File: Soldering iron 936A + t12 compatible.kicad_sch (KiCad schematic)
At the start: 120 parts, among them J1 DC INPUT, J10 Conn_01x01_Socket, J11 Conn_01x01_Socket, J2 USB TO SERIAL, J3 AC input, J4 output_connector, J5 mosfet_driver_future_backup, J6 OLED, J7 USB C BREAKOUT BOARD, J8 Conn_01x01_Socket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

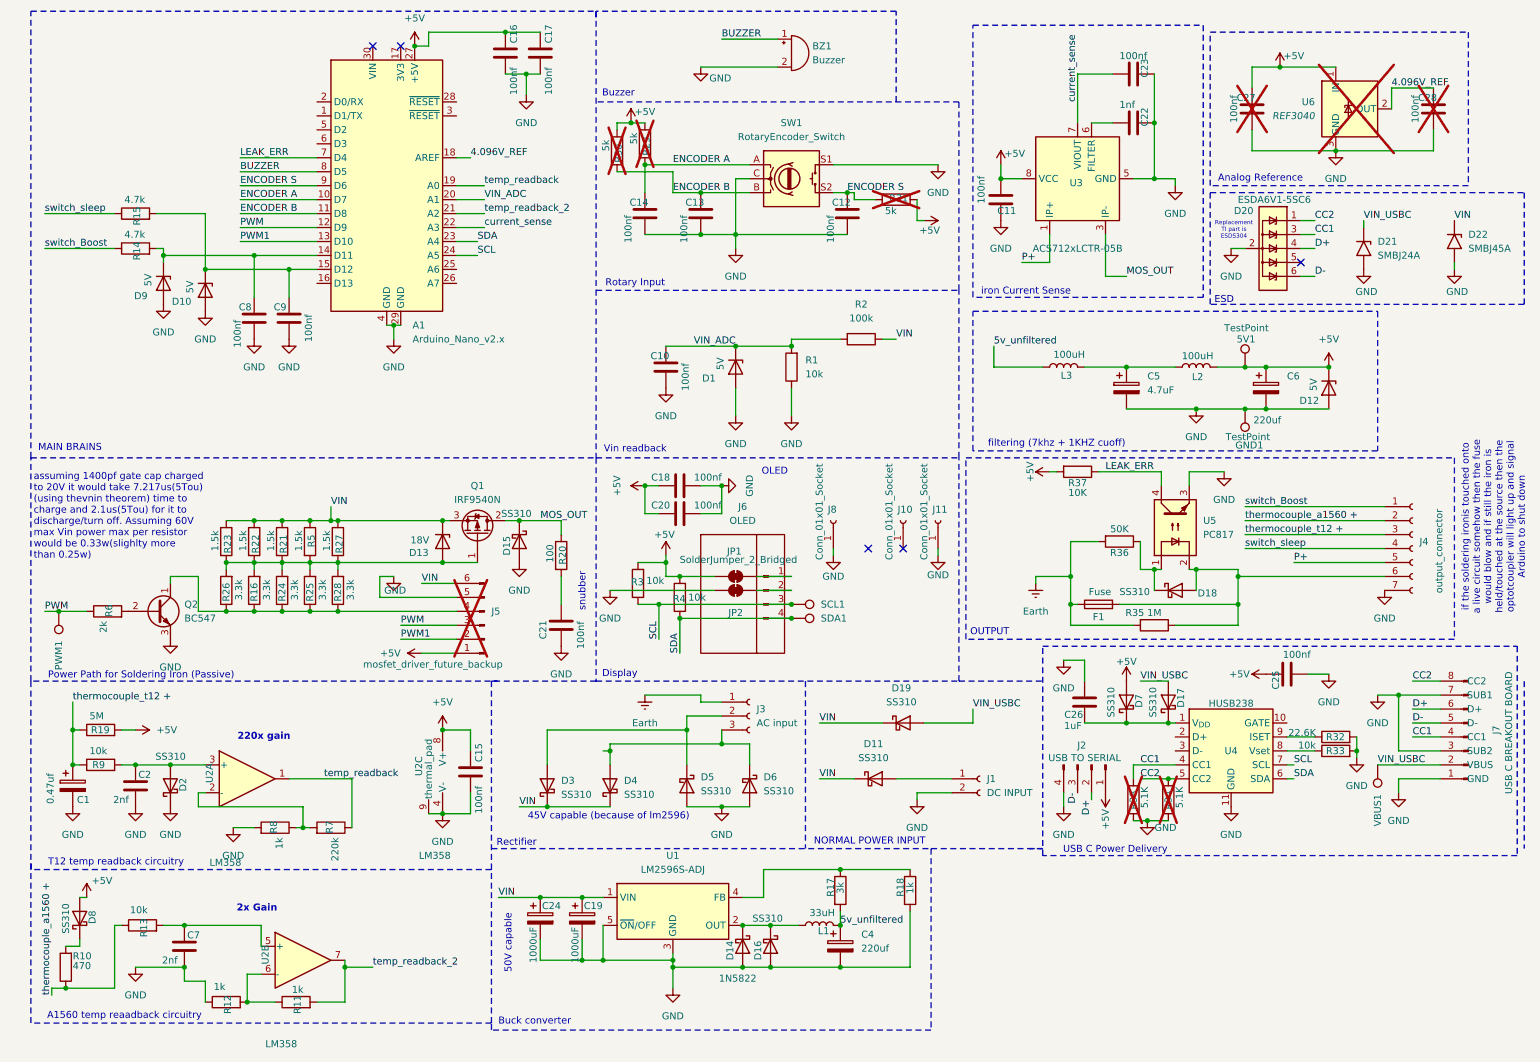
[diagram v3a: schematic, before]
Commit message: Added castellated edges
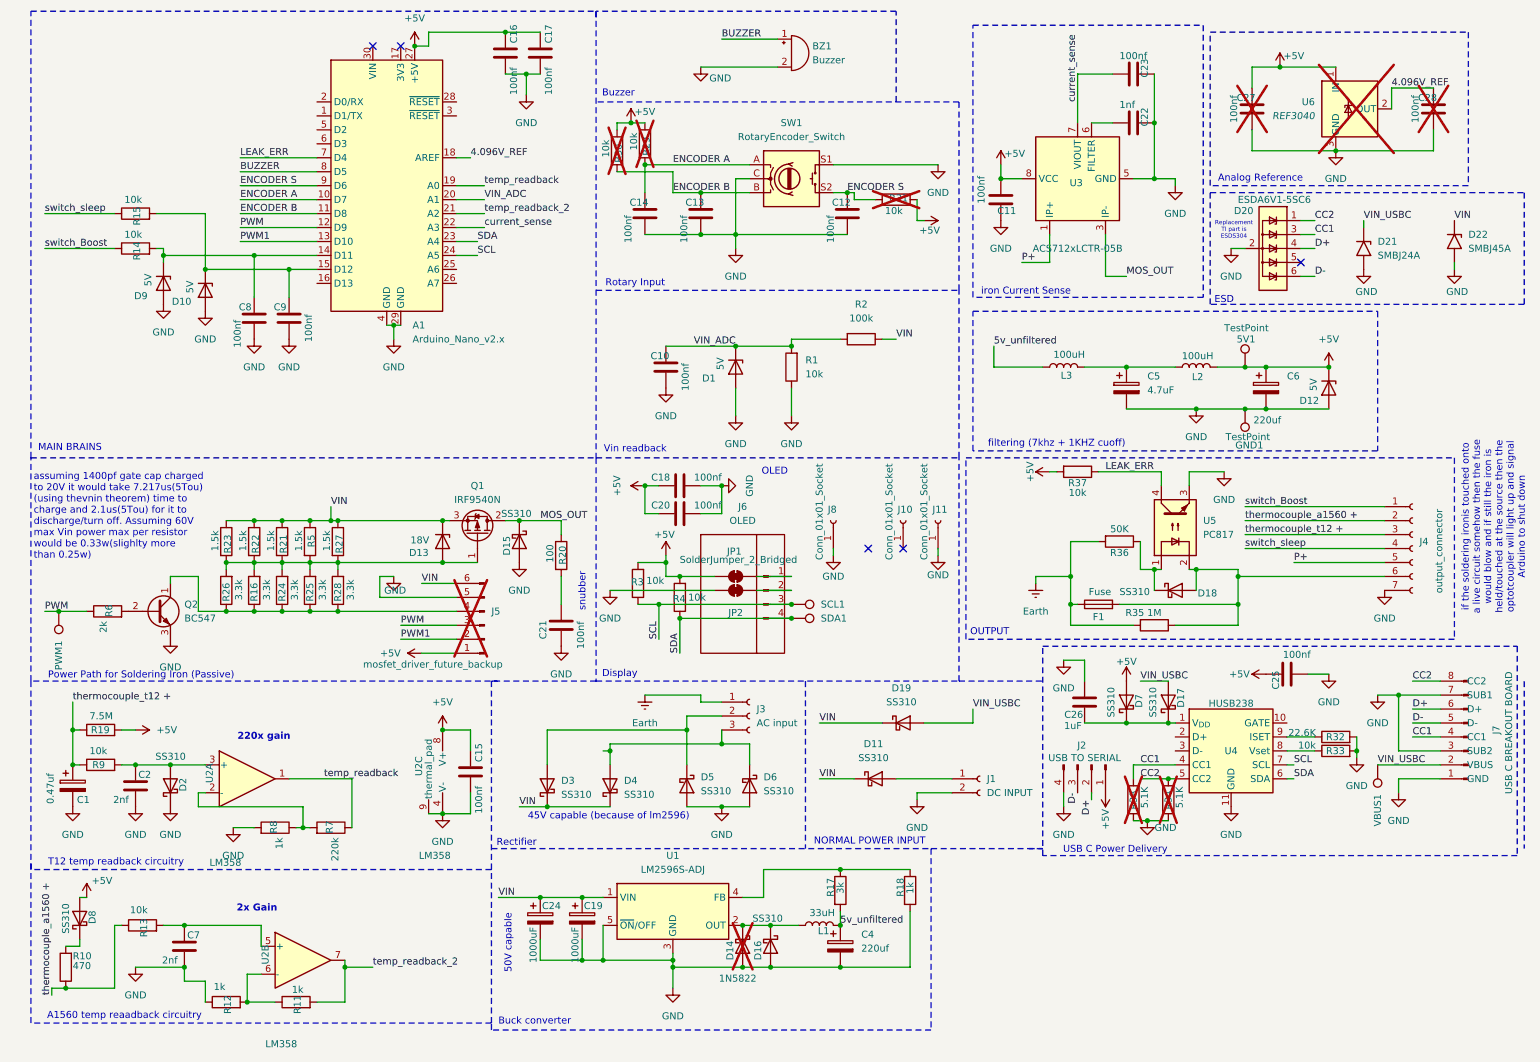
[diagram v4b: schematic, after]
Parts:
- 5V1, C27, C28, GND1, J2, J3, J5, PWM1, R34, R38, SCL1, SDA1, U6, VBUS1: now left out of the parts list
- D14: now not fitted; now left out of the parts list
- R14, R15: value 4.7k -> 10k
- R19: value 5M -> 7.5M
- R29, R30, R31: value 5k -> 10k; now left out of the parts list
- R37: value 10K -> 10k
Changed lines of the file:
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@@
 			)
 		)
-		(property "Value" "4.7k"
+		(property "Value" "10k"
 			(at 29.718 53.34 90)
 			(effects
@@
 			)
 		)
-		(property "Description" "Fuse"
+		(property "Description" "Fuse 1A 1206"
 			(at 207.01 120.65 0)
 			(effects
@@
 			)
 		)
-		(property "Value" "4.7k"
+		(property "Value" "10k"
 			(at 29.718 46.99 90)
 			(effects
@@
 		(unit 1)
 		(exclude_from_sim no)
-		(in_bom yes)
+		(in_bom no)
 		(on_board yes)
 		(dnp yes)
@@
 		(unit 1)
 		(exclude_from_sim no)
-		(in_bom yes)
+		(in_bom no)
 		(on_board yes)
 		(dnp yes)
@@
 			)
 		)
-		(property "Value" "5k"
+		(property "Value" "10k"
 			(at 168.148 49.022 90)
 			(effects
@@
 		(unit 1)
 		(exclude_from_sim no)
-		(in_bom yes)
+		(in_bom no)
 		(on_board yes)
 		(dnp no)
@@
 		(unit 1)
 		(exclude_from_sim no)
-		(in_bom yes)
+		(in_bom no)
 		(on_board yes)
 		(dnp no)
@@
 		(unit 1)
 		(exclude_from_sim no)
-		(in_bom yes)
+		(in_bom no)
 		(on_board yes)
-		(dnp no)
+		(dnp yes)
 		(property "Reference" "D14"
 			(at 139.954 181.864 0)
@@
 		(unit 1)
 		(exclude_from_sim no)
-		(in_bom yes)
+		(in_bom no)
 		(on_board yes)
 		(dnp yes)
@@
 		(unit 1)
 		(exclude_from_sim no)
-		(in_bom yes)
+		(in_bom no)
 		(on_board yes)
 		(dnp yes)
@@
 		(unit 1)
 		(exclude_from_sim no)
-		(in_bom yes)
+		(in_bom no)
 		(on_board yes)
 		(dnp yes)
@@
 			)
 		)
-		(property "Value" "5k"
+		(property "Value" "10k"
 			(at 117.348 36.068 90)
 			(effects
@@
 		(unit 1)
 		(exclude_from_sim no)
-		(in_bom yes)
+		(in_bom no)
 		(on_board yes)
 		(dnp no)
@@
 		(unit 1)
 		(exclude_from_sim no)
-		(in_bom yes)
+		(in_bom no)
 		(on_board yes)
 		(dnp yes)
@@
 		(unit 1)
 		(exclude_from_sim no)
-		(in_bom yes)
+		(in_bom no)
 		(on_board yes)
 		(dnp no)
@@
 		(unit 1)
 		(exclude_from_sim no)
-		(in_bom yes)
+		(in_bom no)
 		(on_board yes)
 		(dnp yes)
@@
 			)
 		)
-		(property "Value" "5k"
+		(property "Value" "10k"
 			(at 122.428 34.798 90)
 			(effects
@@
 		(unit 1)
 		(exclude_from_sim no)
-		(in_bom yes)
+		(in_bom no)
 		(on_board yes)
 		(dnp no)
@@
 		(unit 1)
 		(exclude_from_sim no)
-		(in_bom yes)
+		(in_bom no)
 		(on_board yes)
 		(dnp no)
@@
 		(unit 1)
 		(exclude_from_sim no)
-		(in_bom yes)
+		(in_bom no)
 		(on_board yes)
 		(dnp no)
@@
 		(unit 1)
 		(exclude_from_sim no)
-		(in_bom yes)
+		(in_bom no)
 		(on_board yes)
 		(dnp yes)
@@
 			)
 		)
-		(property "Value" "5M"
+		(property "Value" "7.5M"
 			(at 23.368 140.97 90)
 			(effects
@@
 		(unit 1)
 		(exclude_from_sim no)
-		(in_bom yes)
+		(in_bom no)
 		(on_board yes)
 		(dnp no)
@@
 			)
 		)
-		(property "Value" "10K"
+		(property "Value" "10k"
 			(at 203.2 100.33 90)
 			(effects
@@
 		(unit 1)
 		(exclude_from_sim no)
-		(in_bom yes)
+		(in_bom no)
 		(on_board yes)
 		(dnp yes)

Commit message: Separated Aux Power and Output into different files
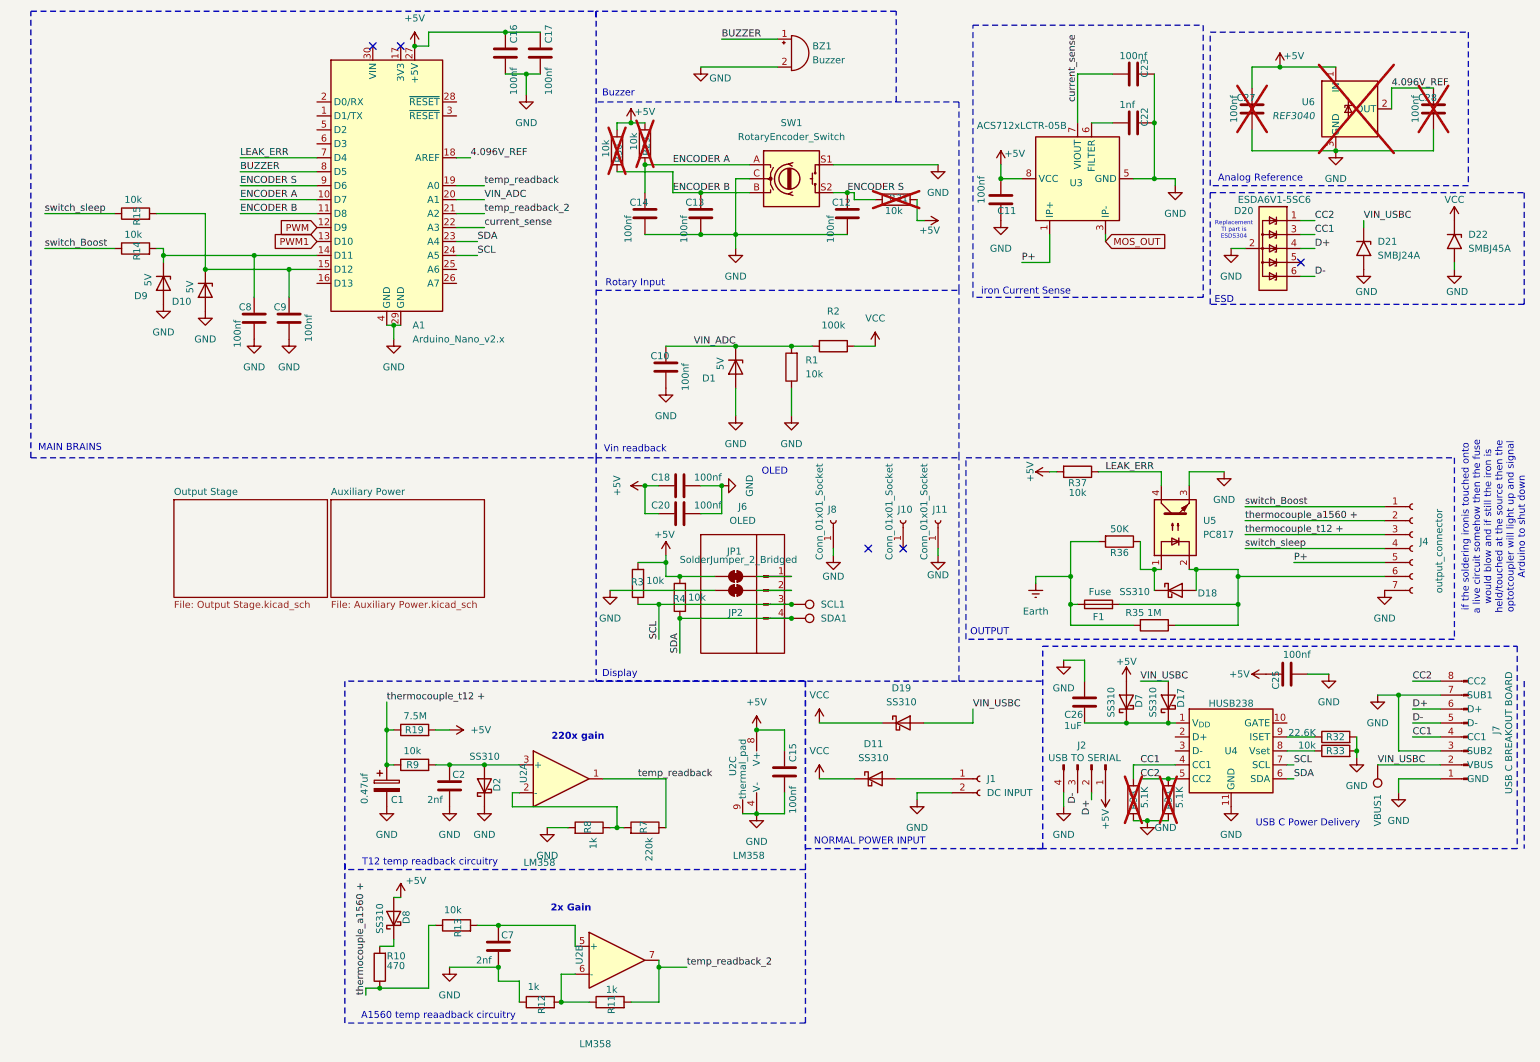
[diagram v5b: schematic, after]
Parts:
- removed 5V1, GND1, PWM1: TestPoint, TestPoint:TestPoint_Pad_D1.0mm, symbol Connector:TestPoint
- removed C19, C24: 1000uF, Capacitor_THT:CP_Radial_D16.0mm_P7.50mm, symbol Device:C_Polarized
- removed C21: 100nf, Capacitor_SMD:C_0603_1608Metric_Pad1.08x0.95mm_HandSolder, symbol Device:C
- removed C4, C6: 220uf, Capacitor_THT:CP_Radial_D8.0mm_P3.80mm, symbol Device:C_Polarized
- removed C5: 4.7uF, Capacitor_THT:CP_Radial_D5.0mm_P2.00mm, symbol Device:C_Polarized
- removed D12: 5V, Diode_THT:D_A-405_P10.16mm_Horizontal, symbol Device:D_Zener
- removed D13: 18V, Diode_THT:D_A-405_P2.54mm_Vertical_KathodeUp, symbol Device:D_Zener
- removed D14: 1N5822, Diode_THT:D_A-405_P10.16mm_Horizontal, symbol Diode:1N5822
- removed D15, D16, D3, D4, D5, D6: SS310, Diode_SMD:D_SMA, symbol Diode:SS310
- removed J3: AC input, Library:BY-G4, symbol Connector:Conn_01x03_Socket
- removed J5: mosfet_driver_future_backup, Connector_PinHeader_2.54mm:PinHeader_1x06_P2.54mm_Vertical, symbol Connector:Conn_01x06_Pin
- removed L1: 33uH, Inductor_SMD:L_12x12mm_H6mm, symbol Device:L
- removed L2, L3: 100uH, Inductor_THT:L_Radial_D7.5mm_P3.50mm_Fastron_07P, symbol Device:L
- removed Q1: IRF9540N, Package_TO_SOT_THT:TO-220-3_Vertical, symbol Transistor_FET:IRF9540N
- removed Q2: BC547, Package_TO_SOT_THT:TO-92_Inline, symbol Transistor_BJT:BC547
- removed R16, R24, R25, R26, R28: 3.3k, Resistor_SMD:R_1206_3216Metric_Pad1.30x1.75mm_HandSolder, symbol Device:R
- removed R17: 3k, Resistor_SMD:R_1206_3216Metric_Pad1.30x1.75mm_HandSolder, symbol Device:R
- removed R18: 1k, Resistor_SMD:R_1206_3216Metric_Pad1.30x1.75mm_HandSolder, symbol Device:R
- removed R20: 100, Resistor_SMD:R_1206_3216Metric_Pad1.30x1.75mm_HandSolder, symbol Device:R
- removed R21, R22, R23, R27, R5: 1.5k, Resistor_SMD:R_1206_3216Metric_Pad1.30x1.75mm_HandSolder, symbol Device:R
- removed R6: 2k, Resistor_SMD:R_1206_3216Metric_Pad1.30x1.75mm_HandSolder, symbol Device:R
- removed U1: LM2596S-ADJ, Package_TO_SOT_SMD:TO-263-5_TabPin3, symbol Regulator_Switching:LM2596S-ADJ
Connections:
- net VIN renamed VCC
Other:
- added sheet Auxiliary Power (Auxiliary Power.kicad_sch)
- added sheet Output Stage (Output Stage.kicad_sch)
- note removed: "45V capable (because of lm2596)"
- note removed: "50V capable"
- note removed: "Buck converter"
- note removed: "Power Path for Soldering Iron (Passive)"
- note removed: "Rectifier"
- note removed: "assuming 1400pf gate cap charged to 20V it would take 7.217us(5Tou) (using thevnin theorem) time to charge and 2.1us(5Tou) for it to discharge/turn off. Assuming 60V max Vin power max per resistor would be 0.33w(slighlty more than 0.25w)"
- note removed: "filtering (7khz + 1KHZ cuoff)"
- note removed: "snubber"
- moved on the sheet: C1, C15, C2, C7, D2, D8, R10, R11, R12, R13, R19, R2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
